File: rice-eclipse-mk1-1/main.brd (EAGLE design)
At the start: 170.1 x 119.4 mm, 193 parts, among them IC1 LMV321LICTRT, IC10 MCP6N11R, IC11 MCP6N11R, IC12 MCP6N11R, IC13 LMV321LICTRT, IC14 LMV321LICTRT, IC15 LMV321LICTRT, IC16 LMV321LICTRT, IC17 LMV321LICTRT, IC2 LMV321LICTRT, IC3 LMV321LICTRT, IC4 LMV321LICTRT, IC5 MCP6N11R, IC6 LMV321LICTRT, IC7 LMV321LICTRT, IC8 LMV321LICTRT, IC9 LMV321LICTRT, U6 1101M2S3CQE2

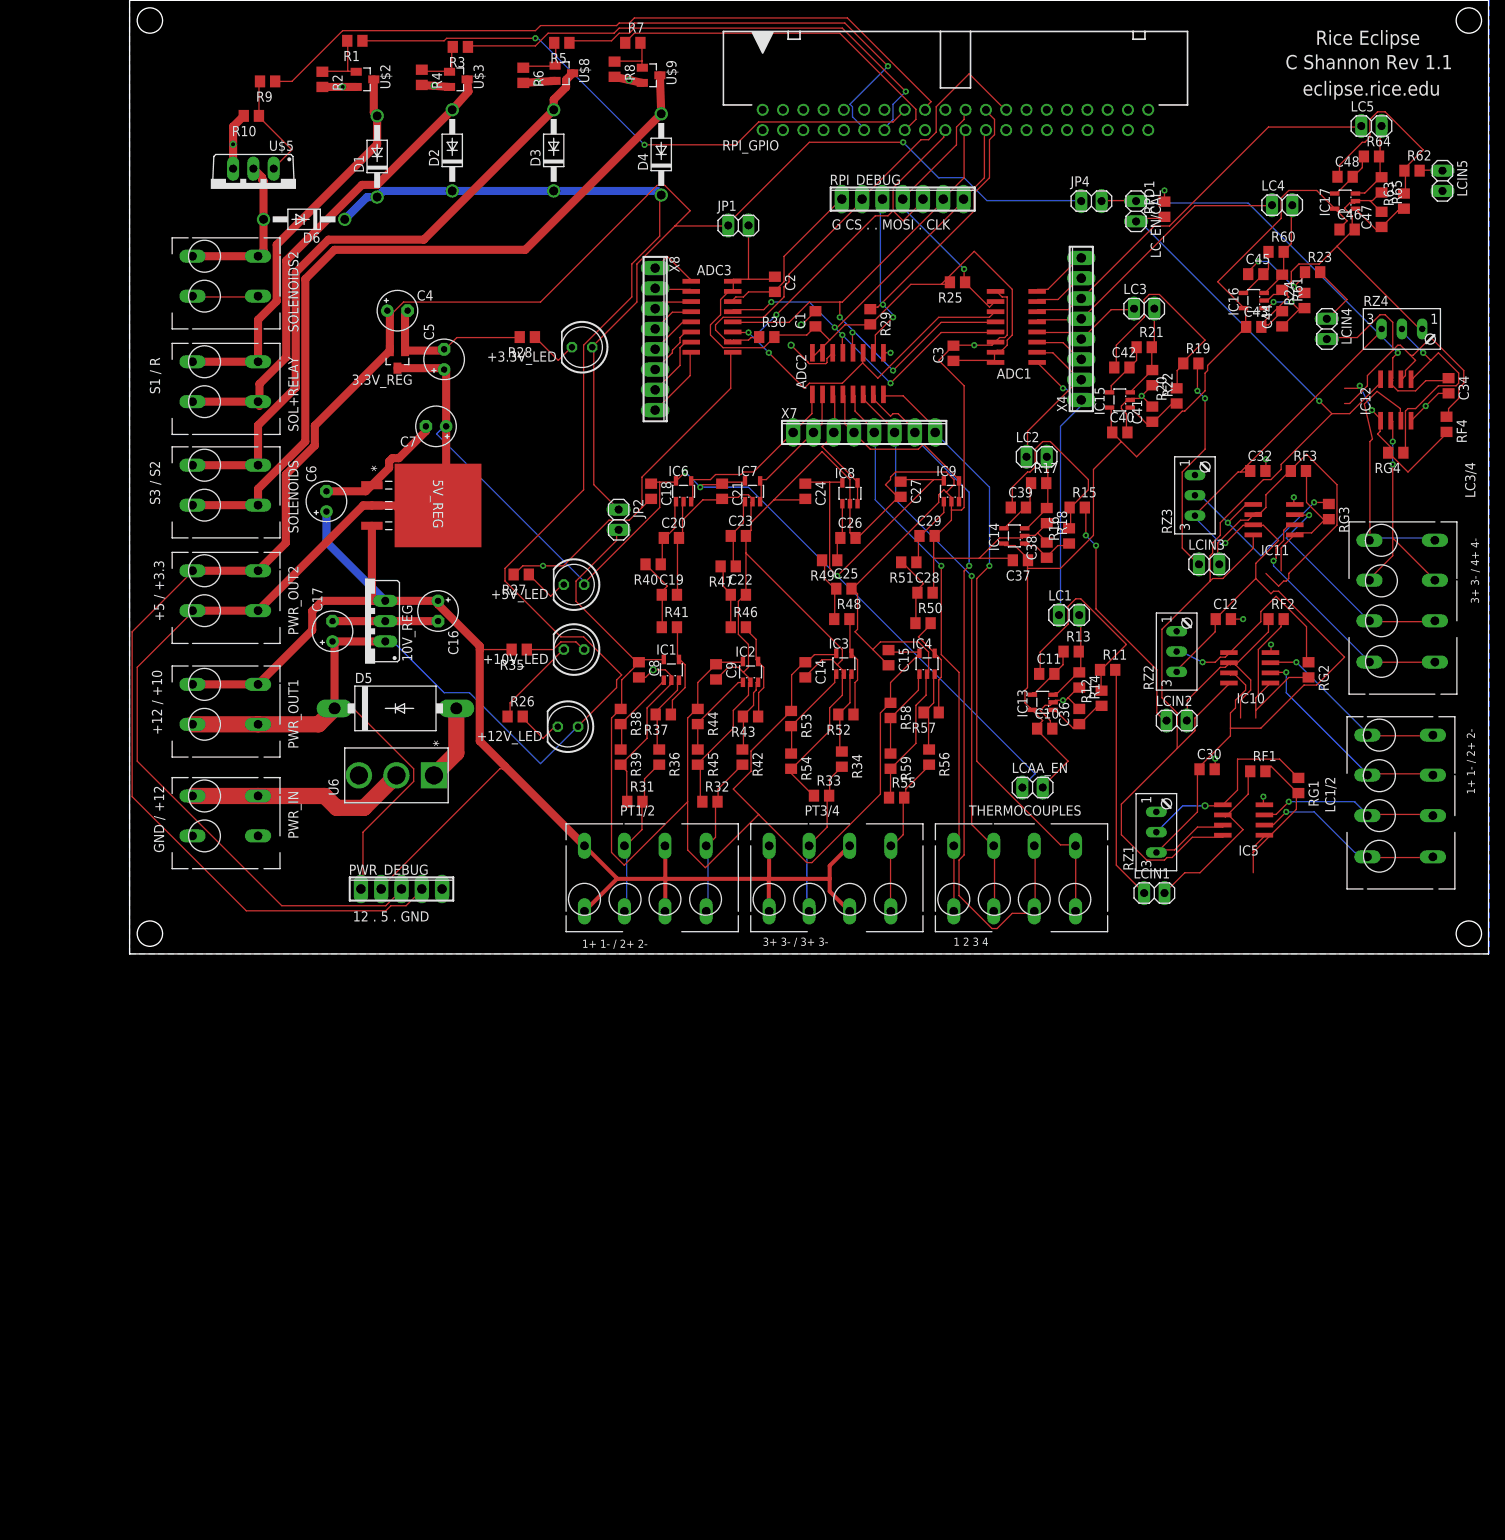
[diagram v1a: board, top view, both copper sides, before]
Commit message: Make files match IRL
- Fix jumpers to take output of the op amp
directly, instead of across a resistor

- Changed adc inputs to 3.3V from 5V

- Added larger mosfets for TVC valves,
need to double check though.

Todo:
- Add igniter profiling circuitry

- Route the board
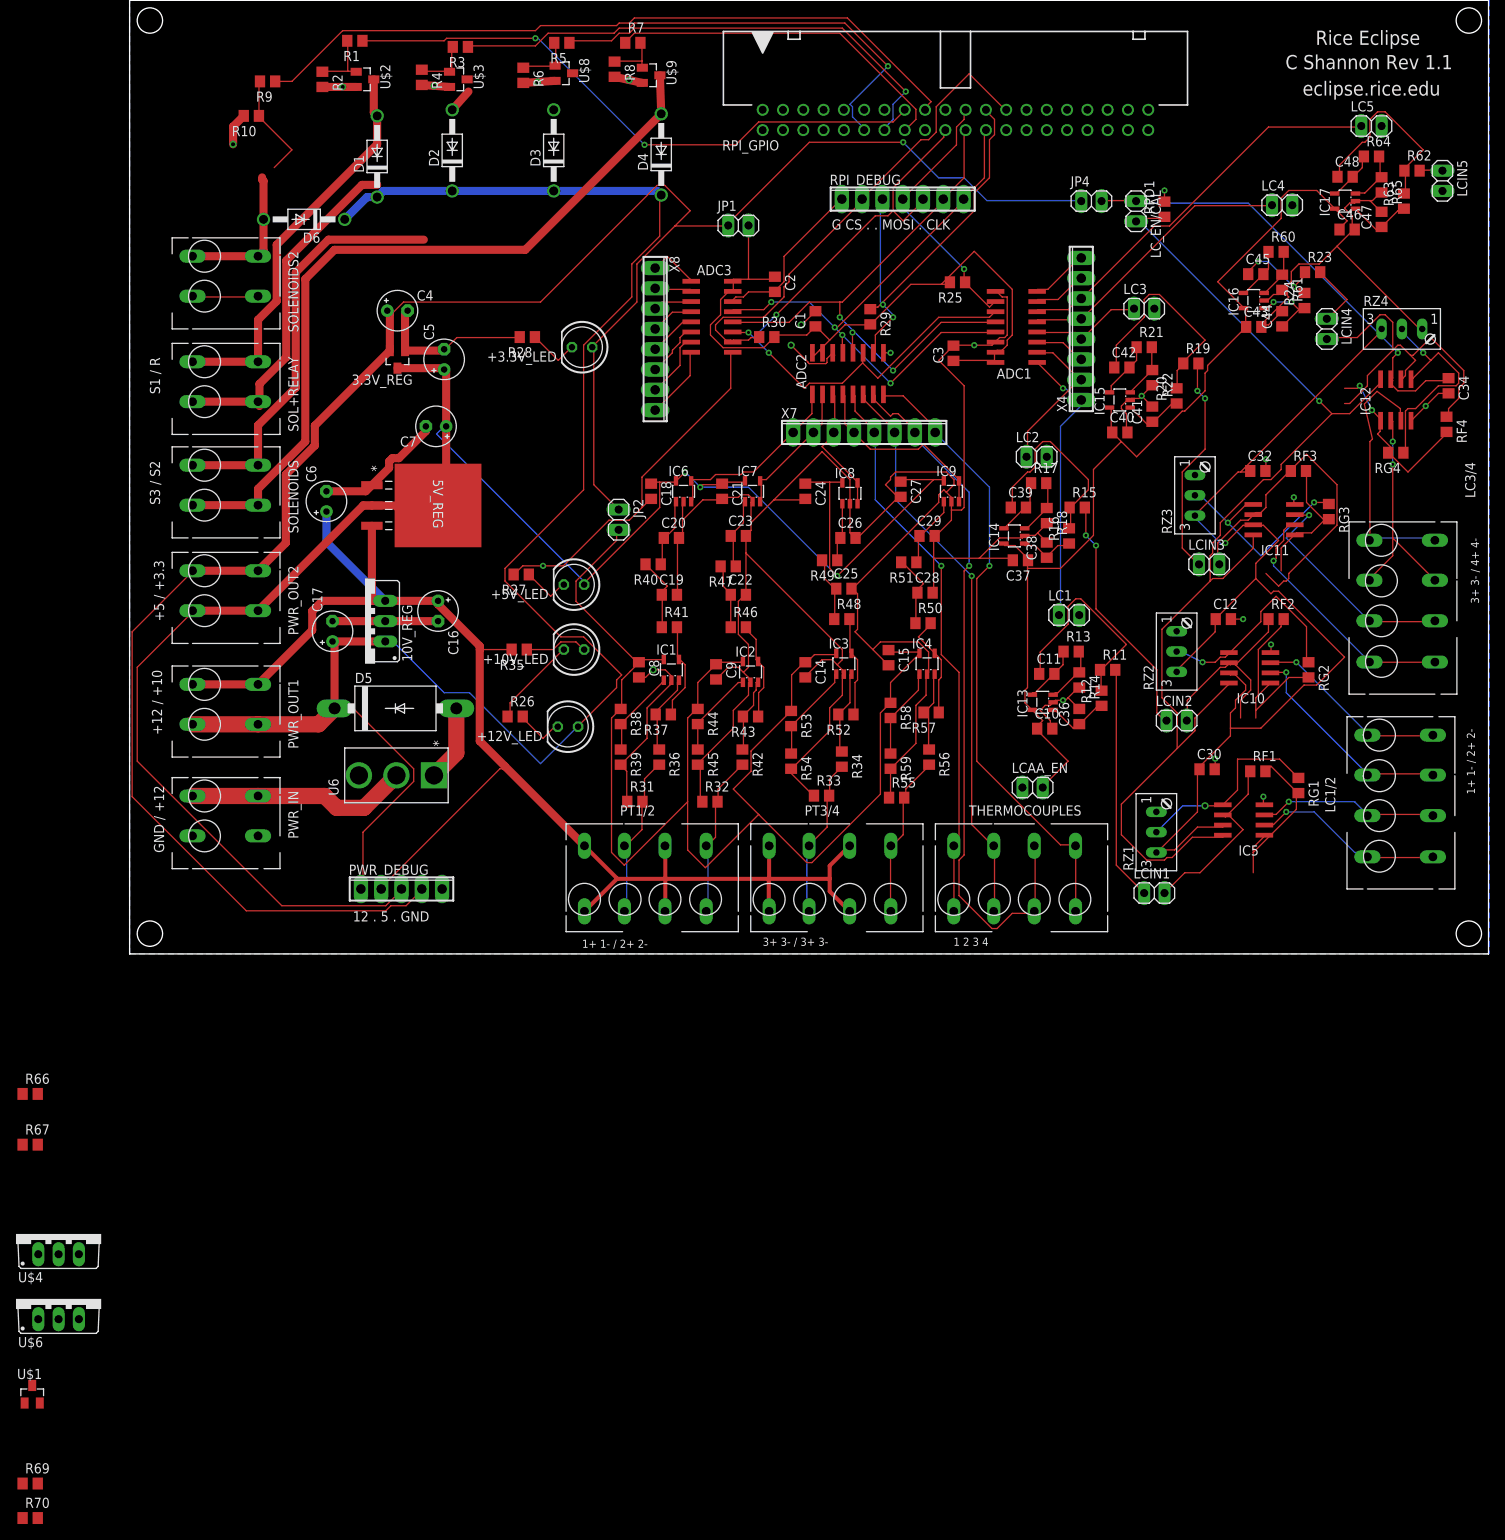
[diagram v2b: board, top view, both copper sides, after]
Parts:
- removed U$5: IRF740, transistor-power:TO220BV
- added R66, R67, R69, R70: (no value), rcl:R0805
- added U$1: 2N7000, transistor-fet-extra:SOT23
- added U$4, U$6: IRF740, transistor-power:TO220BV
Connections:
- new net +3V3_LCAA: C10.1, IC13.5, LCAA_EN.2
- new net N$61: R70.2, U$3.3, U$6.G
- new net N$63: R69.2, U$4.G, U$8.3
- net +12V: now also R66.2, R67.2, R69.1, R70.1
- net +3V3: now also LCAA_EN.1
- net +5V: no longer LCAA_EN.1
- net +5V_LCAA: no longer C10.1, IC13.5, LCAA_EN.2
- net GND: now also U$1.2, U$4.S, U$6.S; no longer U$5.S
- net N$14: now also U$1.1; no longer U$5.G
- net N$18: now also LC1.2
- net N$20: now also LC2.2
- net N$23: no longer LC2.2
- net N$40: now also LC3.2
- net N$44: no longer LC3.2
- net N$49: now also LC4.2
- net N$50: no longer LC1.2
- net N$51: no longer LC4.2
- net N$58: now also LC5.2
- net N$59: no longer LC5.2
- net SOLENOID_1_NEGATIVE: now also R66.1, U$6.D; no longer U$3.3
- net SOLENOID_2_NEGATIVE: now also R67.1, U$4.D; no longer U$8.3
- net SOLENOID_4_NEGATIVE: now also U$1.3; no longer U$5.D
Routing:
- net +5V: track 285.5 -> 248.1 mm
- net SOLENOID_2_NEGATIVE: track 80.6 -> 52.0 mm
- net SOLENOID_1_NEGATIVE: track 61.2 -> 46.4 mm
- net +5V_LCAA: track 122.6 -> 108.4 mm
- net +3V3_LCAA: track 0.00 -> 13.7 mm
- net N$51: track 12.5 -> 6.29 mm
- net N$50: track 12.2 -> 7.78 mm
- net N$44: track 11.8 -> 7.50 mm
- net N$59: track 10.8 -> 7.03 mm
- net N$23: track 10.7 -> 7.35 mm
- net GND: track 570.9 -> 567.9 mm
- net SOLENOID_4_NEGATIVE: track 20.0 -> 18.4 mm

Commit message: Add mosfet driver circuit
Currently have a version with a switch for using either
the 2N7000 or IRF740 (high current). Might be useful to
have a high current option for all the outputs since
propulsion seems to like adding more high-current valves.
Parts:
- added D7, D8, D9: 1N4004, diode:DO41-10
- added R68: 10k, rcl:R0805
- added R71: 500k, rcl:R0805
- added R72, R73: (no value), rcl:R0805
- added R74: 0.005, rcl:R0805
- added U$5: 2N7000, transistor-fet-extra:SOT23
- added U$7: IRF740, transistor-power:TO220BV
- added U2: 1101M2S3CQE2, SLIDE_SW:1101M2S3CQE2
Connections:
- new net N$62: R68.2, R71.1, U$5.1
- new net N$64: U$5.3, U2.2
- new net N$65: R72.1, U$7.G, U2.3
- new net N$66: D9.A, R73.1, U$7.D
- new net N$67: R74.1, U$9.3
- net +12V: now also D7.C, D8.C, D9.C, R70.2, R72.2, R73.2; no longer R70.1
- net CTRL_SOLENOID_3: now also R68.1
- net GND: now also R71.2, U$5.2, U$7.S
- net N$61: now also D7.A, R70.1; no longer R70.2
- net SOLENOID_3_NEGATIVE: now also D8.A, R74.2, U2.1; no longer U$9.3
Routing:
- net SOLENOID_3_NEGATIVE: track 96.9 -> 92.1 mm
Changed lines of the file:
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@@
 <attribute name="VALUE" x="-13.081" y="-73.152" size="1.27" layer="27"/>
 </element>
+<element name="D7" library="diode" library_urn="urn:adsk.eagle:library:210" package="DO41-10" package3d_urn="urn:adsk.eagle:package:43336/1" value="1N4004" x="-8.382" y="-75.184" smashed="yes">
+<attribute name="NAME" x="-10.414" y="-73.533" size="1.27" layer="25" ratio="10"/>
+<attribute name="VALUE" x="-10.414" y="-77.978" size="1.27" layer="27" ratio="10"/>
+</element>
+<element name="U2" library="SLIDE_SW" package="1101M2S3CQE2" value="1101M2S3CQE2" x="-18.288" y="-89.916" smashed="yes">
+<attribute name="COPYRIGHT" value="Copyright (C) 2015 Accelerated Designs. All rights reserved" x="-26.924" y="-73.914" size="1.778" layer="27" display="off"/>
+<attribute name="MANUFACTURER_PART_NUMBER" value="1101M2S3CQE2" x="-26.924" y="-73.914" size="1.778" layer="27" display="off"/>
+<attribute name="NAME" x="-15.748" y="-92.456" size="1.27" layer="21" ratio="6" rot="R180"/>
+<attribute name="VENDOR" value="C&amp;K" x="-26.924" y="-73.914" size="1.778" layer="27" display="off"/>
+</element>
+<element name="U$5" library="transistor-fet-extra" package="SOT23" value="2N7000" x="-20.574" y="-98.044" smashed="yes">
+<attribute name="NAME" x="-22.479" y="-96.139" size="1.27" layer="25"/>
+<attribute name="VALUE" x="-22.479" y="-101.219" size="1.27" layer="27"/>
+</element>
+<element name="R68" library="rcl" library_urn="urn:adsk.eagle:library:334" package="R0805" value="10k" x="-15.24" y="-112.014" smashed="yes">
+<attribute name="NAME" x="-15.875" y="-110.744" size="1.27" layer="25"/>
+<attribute name="VALUE" x="-15.875" y="-114.554" size="1.27" layer="27"/>
+</element>
+<element name="R71" library="rcl" library_urn="urn:adsk.eagle:library:334" package="R0805" value="500k" x="-21.082" y="-112.014" smashed="yes">
+<attribute name="NAME" x="-21.717" y="-110.744" size="1.27" layer="25"/>
+<attribute name="VALUE" x="-21.717" y="-114.554" size="1.27" layer="27"/>
+</element>
+<element name="D8" library="diode" library_urn="urn:adsk.eagle:library:210" package="DO41-10" package3d_urn="urn:adsk.eagle:package:43336/1" value="1N4004" x="-17.018" y="-105.41" smashed="yes">
+<attribute name="NAME" x="-19.05" y="-103.759" size="1.27" layer="25" ratio="10"/>
+<attribute name="VALUE" x="-19.05" y="-108.204" size="1.27" layer="27" ratio="10"/>
+</element>
+<element name="U$7" library="transistor-power" library_urn="urn:adsk.eagle:library:400" package="TO220BV" package3d_urn="urn:adsk.eagle:package:29484/3" value="IRF740" x="-17.526" y="-115.062" smashed="yes">
+<attribute name="NAME" x="-22.606" y="-121.1072" size="1.27" layer="25" ratio="10"/>
+<attribute name="VALUE" x="-22.606" y="-122.682" size="1.27" layer="27" ratio="10"/>
+</element>
+<element name="D9" library="diode" library_urn="urn:adsk.eagle:library:210" package="DO41-10" package3d_urn="urn:adsk.eagle:package:43336/1" value="1N4004" x="-17.018" y="-126.746" smashed="yes">
+<attribute name="NAME" x="-19.05" y="-125.095" size="1.27" layer="25" ratio="10"/>
+<attribute name="VALUE" x="-19.05" y="-129.54" size="1.27" layer="27" ratio="10"/>
+</element>
+<element name="R72" library="rcl" library_urn="urn:adsk.eagle:library:334" package="R0805" value="" x="-21.082" y="-133.35" smashed="yes">
+<attribute name="NAME" x="-21.717" y="-132.08" size="1.27" layer="25"/>
+<attribute name="VALUE" x="-21.717" y="-135.89" size="1.27" layer="27"/>
+</element>
+<element name="R73" library="rcl" library_urn="urn:adsk.eagle:library:334" package="R0805" value="" x="-24.13" y="-137.668" smashed="yes">
+<attribute name="NAME" x="-24.765" y="-136.398" size="1.27" layer="25"/>
+<attribute name="VALUE" x="-24.765" y="-140.208" size="1.27" layer="27"/>
+</element>
+<element name="R74" library="rcl" library_urn="urn:adsk.eagle:library:334" package="R0805" value="0.005" x="-24.13" y="-141.986" smashed="yes">
+<attribute name="NAME" x="-24.765" y="-140.716" size="1.27" layer="25"/>
+<attribute name="VALUE" x="-24.765" y="-144.526" size="1.27" layer="27"/>
+</element>
 </elements>
 <signals>
@@
 <contactref element="U$6" pad="S"/>
 <contactref element="U$4" pad="S"/>
+<contactref element="R71" pad="2"/>
+<contactref element="U$5" pad="2"/>
+<contactref element="U$7" pad="S"/>
 <wire x1="161.6075" y1="78.105" x2="163.83" y2="70.1675" width="0" layer="19" extent="1-1"/>
 <wire x1="128.016" y1="71.186" x2="141.666" y2="78.486" width="0" layer="19" extent="1-1"/>
@@
 <wire x1="-6.35" y1="-45.72" x2="-6.35" y2="-37.592" width="0" layer="19" extent="1-1"/>
 <wire x1="-11.242" y1="-56.218" x2="-6.35" y2="-45.72" width="0" layer="19" extent="1-1"/>
+<wire x1="-19.624" y1="-99.144" x2="-11.242" y2="-56.218" width="0" layer="19" extent="1-1"/>
+<wire x1="-20.132" y1="-112.014" x2="-19.624" y2="-99.144" width="0" layer="19" extent="1-1"/>
+<wire x1="-14.986" y1="-117.602" x2="-20.132" y2="-112.014" width="0" layer="19" extent="1-1"/>
 </signal>
 <signal name="+12V">
@@
 <contactref element="R66" pad="2"/>
 <contactref element="R67" pad="2"/>
-<contactref element="R70" pad="1"/>
 <contactref element="R69" pad="1"/>
-<wire x1="-13.396" y1="-66.294" x2="-13.396" y2="-70.612" width="0" layer="19" extent="1-1"/>
+<contactref element="D7" pad="C"/>
+<contactref element="R70" pad="2"/>
+<contactref element="D8" pad="C"/>
+<contactref element="R72" pad="2"/>
+<contactref element="D9" pad="C"/>
+<contactref element="R73" pad="2"/>
+<wire x1="-20.132" y1="-133.35" x2="-23.18" y2="-137.668" width="0" layer="19" extent="1-1"/>
+<wire x1="-22.098" y1="-126.746" x2="-20.132" y2="-133.35" width="0" layer="19" extent="1-1"/>
+<wire x1="-22.098" y1="-105.41" x2="-22.098" y2="-126.746" width="0" layer="19" extent="1-1"/>
+<wire x1="-13.462" y1="-75.184" x2="-22.098" y2="-105.41" width="0" layer="19" extent="1-1"/>
+<wire x1="-11.496" y1="-70.612" x2="-13.462" y2="-75.184" width="0" layer="19" extent="1-1"/>
+<wire x1="-13.396" y1="-66.294" x2="-11.496" y2="-70.612" width="0" layer="19" extent="1-1"/>
 <wire x1="-11.496" y1="-23.876" x2="-13.396" y2="-66.294" width="0" layer="19" extent="1-1"/>
 <wire x1="-11.496" y1="-17.526" x2="-11.496" y2="-23.876" width="0" layer="19" extent="1-1"/>
@@
 <wire x1="62.23" y1="114.3" x2="62.042" y2="114.046" width="0.1524" layer="1"/>
 <wire x1="97.155" y1="103.1875" x2="97.028" y2="103.124" width="0.1524" layer="1"/>
+<contactref element="R68" pad="1"/>
+<wire x1="-16.19" y1="-112.014" x2="62.042" y2="114.046" width="0" layer="19" extent="1-1"/>
 </signal>
 <signal name="SOLENOID_3_NEGATIVE">
-<contactref element="U$9" pad="3"/>
 <contactref element="SOLENOIDS" pad="A2"/>
 <contactref element="SOLENOIDS" pad="B2"/>
 <contactref element="D4" pad="A"/>
 <wire x1="7.874" y1="56.174" x2="16.074" y2="56.174" width="1.016" layer="1"/>
-<wire x1="66.548" y1="105.156" x2="66.378" y2="109.982" width="1.016" layer="1"/>
 <wire x1="66.548" y1="105.156" x2="49.53" y2="88.138" width="1.016" layer="1"/>
 <wire x1="49.53" y1="88.138" x2="25.654" y2="88.138" width="1.016" layer="1"/>
@@
 <wire x1="21.9912" y1="84.4752" x2="21.9912" y2="64.1296" width="1.016" layer="1"/>
 <wire x1="21.9912" y1="64.1296" x2="16.074" y2="58.2124" width="1.016" layer="1"/>
+<contactref element="D8" pad="A"/>
+<contactref element="U2" pad="1"/>
+<contactref element="R74" pad="2"/>
+<wire x1="-11.938" y1="-105.41" x2="-23.18" y2="-141.986" width="0" layer="19" extent="1-1"/>
+<wire x1="-18.288" y1="-80.518" x2="-11.938" y2="-105.41" width="0" layer="19" extent="1-1"/>
+<wire x1="7.874" y1="56.174" x2="-18.288" y2="-80.518" width="0" layer="19" extent="1-1"/>
 </signal>
 <signal name="N$5">
@@
 <signal name="N$61">
 <contactref element="U$3" pad="3"/>
-<contactref element="R70" pad="2"/>
+<contactref element="D7" pad="A"/>
+<contactref element="R70" pad="1"/>
 <contactref element="U$6" pad="G"/>
 <wire x1="-11.43" y1="-45.72" x2="42.248" y2="109.474" width="0" layer="19" extent="1-1"/>
-<wire x1="-11.496" y1="-70.612" x2="-11.43" y2="-45.72" width="0" layer="19" extent="1-1"/>
+<wire x1="-13.396" y1="-70.612" x2="-11.43" y2="-45.72" width="0" layer="19" extent="1-1"/>
+<wire x1="-3.302" y1="-75.184" x2="-13.396" y2="-70.612" width="0" layer="19" extent="1-1"/>
 </signal>
 <signal name="N$63">
@@
 <wire x1="-11.496" y1="-66.294" x2="-11.43" y2="-37.592" width="0" layer="19" extent="1-1"/>
 </signal>
+<signal name="N$62">
+<contactref element="R68" pad="2"/>
+<contactref element="U$5" pad="1"/>
+<contactref element="R71" pad="1"/>
+<wire x1="-14.29" y1="-112.014" x2="-22.032" y2="-112.014" width="0" layer="19" extent="1-1"/>
+<wire x1="-21.524" y1="-99.144" x2="-22.032" y2="-112.014" width="0" layer="19" extent="1-1"/>
+</signal>
+<signal name="N$64">
+<contactref element="U$5" pad="3"/>
+<contactref element="U2" pad="2"/>
+<wire x1="-18.288" y1="-85.217" x2="-20.574" y2="-96.944" width="0" layer="19" extent="1-1"/>
+</signal>
+<signal name="N$65">
+<contactref element="U2" pad="3"/>
+<contactref element="U$7" pad="G"/>
+<contactref element="R72" pad="1"/>
+<wire x1="-20.066" y1="-117.602" x2="-22.032" y2="-133.35" width="0" layer="19" extent="1-1"/>
+<wire x1="-18.288" y1="-89.916" x2="-20.066" y2="-117.602" width="0" layer="19" extent="1-1"/>
+</signal>
+<signal name="N$66">
+<contactref element="D9" pad="A"/>
+<contactref element="U$7" pad="D"/>
+<contactref element="R73" pad="1"/>
+<wire x1="-11.938" y1="-126.746" x2="-25.08" y2="-137.668" width="0" layer="19" extent="1-1"/>
+<wire x1="-17.526" y1="-117.602" x2="-11.938" y2="-126.746" width="0" layer="19" extent="1-1"/>
+</signal>
+<signal name="N$67">
+<contactref element="R74" pad="1"/>
+<contactref element="U$9" pad="3"/>
+<wire x1="-25.08" y1="-141.986" x2="66.378" y2="109.982" width="0" layer="19" extent="1-1"/>
+</signal>
 </signals>
